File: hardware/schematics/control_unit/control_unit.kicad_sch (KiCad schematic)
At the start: 10 parts, among them J1 Screw_Terminal_01x12, J2 Screw_Terminal_01x08, J3 Screw_Terminal_01x08, J4 AudioJack4, J5 Screw_Terminal_01x08, J6 6P6C, J7 Conn_01x03_Pin, J8 Conn_01x03_Pin

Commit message: !feat
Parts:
- added H1, H2, H3, H4: MountingHole, MountingHole:MountingHole_4.5mm_Pad_TopBottom, symbol Mechanical:MountingHole
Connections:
- net GND: now also JP1.3 (B); no longer JP1.1 (A)
- net MCU/DE/~{RE}: now also JP1.1 (A); no longer JP1.3 (B)

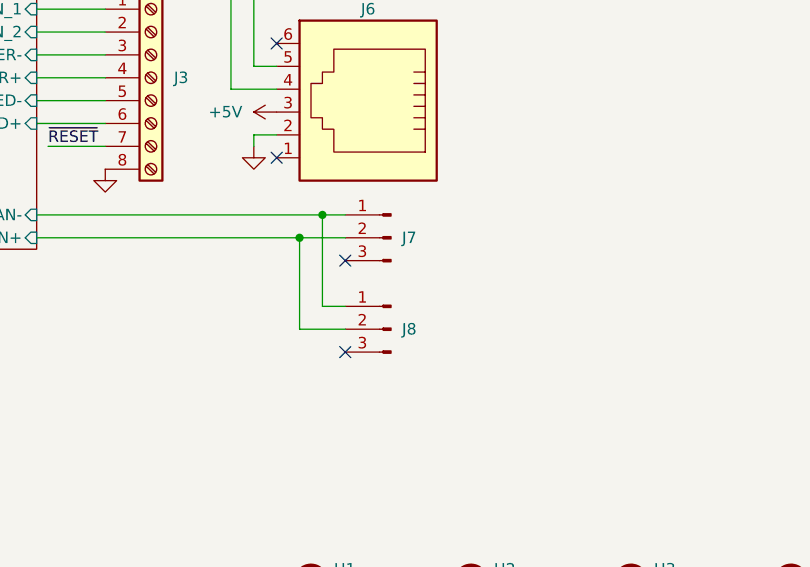
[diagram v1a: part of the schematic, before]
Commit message: feat: final PCB topological design.
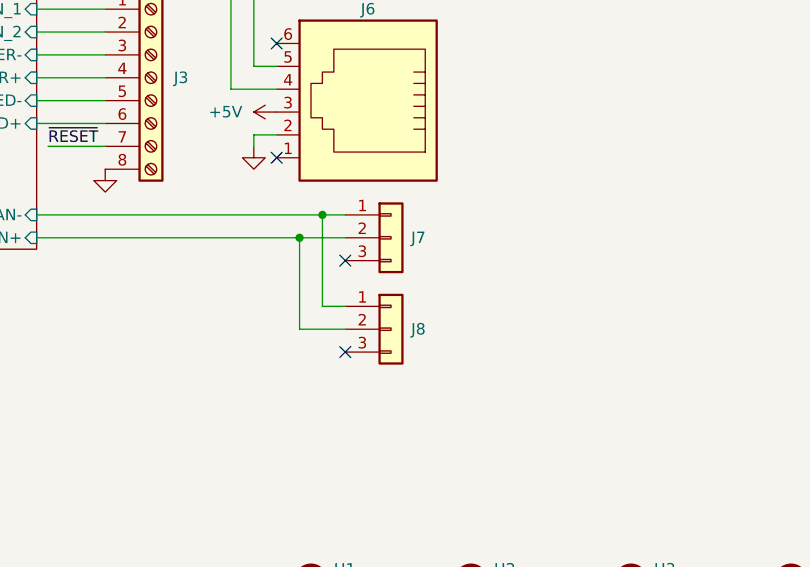
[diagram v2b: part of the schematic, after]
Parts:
- J7, J8: symbol Connector:Conn_01x03_Pin -> Connector_Generic:Conn_01x03
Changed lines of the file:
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@@
 	)
 	(symbol
-		(lib_id "Connector:Conn_01x03_Pin")
+		(lib_id "Connector_Generic:Conn_01x03")
 		(at 187.96 124.46 0)
-		(mirror y)
 		(unit 1)
 		(exclude_from_sim no)
@@
 		(dnp no)
 		(property "Reference" "J7"
-			(at 189.992 124.46 0)
+			(at 191.008 124.46 0)
 			(effects
 				(font
@@
 		)
 		(property "Value" "Conn_01x03_Pin"
-			(at 187.325 119.38 0)
+			(at 188.595 119.38 0)
 			(effects
 				(font
@@
 			)
 		)
-		(property "Description" "Generic connector, single row, 01x03, script generated"
+		(property "Description" "Generic connector, single row, 01x03, script generated (kicad-library-utils/schlib/autogen/connector/)"
 			(at 187.96 124.46 0)
 			(effects
@@
 	)
 	(symbol
-		(lib_id "Connector:Conn_01x03_Pin")
+		(lib_id "Connector_Generic:Conn_01x03")
 		(at 187.96 134.62 0)
-		(mirror y)
 		(unit 1)
 		(exclude_from_sim no)
@@
 		(dnp no)
 		(property "Reference" "J8"
-			(at 189.992 134.62 0)
+			(at 191.008 134.62 0)
 			(effects
 				(font
@@
 		)
 		(property "Value" "Conn_01x03_Pin"
-			(at 187.325 129.54 0)
+			(at 188.595 129.54 0)
 			(effects
 				(font
@@
 			)
 		)
-		(property "Description" "Generic connector, single row, 01x03, script generated"
+		(property "Description" "Generic connector, single row, 01x03, script generated (kicad-library-utils/schlib/autogen/connector/)"
 			(at 187.96 134.62 0)
 			(effects

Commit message: !feat: control_unit first PCB release.
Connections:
- net GND: now also J5.5 (Pin_5), J5.7 (Pin_7)
- net at F1.1, J5.3 (Pin_3): no longer J5.5 (Pin_5), J5.7 (Pin_7)
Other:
- moved on the sheet: F1
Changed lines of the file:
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@@
+	)
+	(junction
+		(at 165.1 36.83)
+		(diameter 0)
+		(color 0 0 0 0)
 	)
 	(junction
@@
 	)
 	(junction
-		(at 165.1 36.83)
-		(diameter 0)
-		(color 0 0 0 0)
-	)
-	(junction
 		(at 119.38 121.92)
 		(diameter 0)
@@
 	(wire
 		(pts
+			(xy 168.91 26.67) (xy 165.1 26.67)
+		)
+		(stroke
+			(width 0)
+			(type default)
+		)
+	)
+	(wire
+		(pts
 			(xy 165.1 41.91) (xy 176.53 41.91)
 		)
@@
 	(wire
 		(pts
+			(xy 165.1 26.67) (xy 165.1 27.94)
+		)
+		(stroke
+			(width 0)
+			(type default)
+		)
+	)
+	(wire
+		(pts
 			(xy 148.59 91.44) (xy 172.72 91.44)
 		)
@@
 	(wire
 		(pts
-			(xy 176.53 31.75) (xy 165.1 31.75)
-		)
-		(stroke
-			(width 0)
-			(type default)
-		)
-	)
-	(wire
-		(pts
 			(xy 53.34 44.45) (xy 63.5 44.45)
 		)
@@
 	(wire
 		(pts
+			(xy 168.91 31.75) (xy 168.91 26.67)
+		)
+		(stroke
+			(width 0)
+			(type default)
+		)
+	)
+	(wire
+		(pts
 			(xy 148.59 101.6) (xy 156.21 101.6)
 		)
@@
 	(wire
 		(pts
+			(xy 165.1 35.56) (xy 165.1 36.83)
+		)
+		(stroke
+			(width 0)
+			(type default)
+		)
+	)
+	(wire
+		(pts
 			(xy 177.8 124.46) (xy 182.88 124.46)
 		)
@@
 	(wire
 		(pts
-			(xy 167.64 26.67) (xy 176.53 26.67)
+			(xy 171.45 26.67) (xy 176.53 26.67)
 		)
 		(stroke
@@
 	(wire
 		(pts
-			(xy 167.64 29.21) (xy 176.53 29.21)
+			(xy 171.45 29.21) (xy 176.53 29.21)
 		)
 		(stroke
@@
 	(wire
 		(pts
+			(xy 176.53 31.75) (xy 168.91 31.75)
+		)
+		(stroke
+			(width 0)
+			(type default)
+		)
+	)
+	(wire
+		(pts
 			(xy 111.76 64.77) (xy 121.92 64.77)
 		)
@@
 	(wire
 		(pts
-			(xy 165.1 31.75) (xy 165.1 36.83)
-		)
-		(stroke
-			(width 0)
-			(type default)
-		)
-	)
-	(wire
-		(pts
 			(xy 165.1 41.91) (xy 165.1 45.72)
 		)
@@
 	)
 	(label "AC_N"
-		(at 167.64 29.21 0)
+		(at 171.45 29.21 0)
 		(fields_autoplaced yes)
 		(effects
@@
 	)
 	(label "AC_L"
-		(at 167.64 26.67 0)
+		(at 171.45 26.67 0)
 		(fields_autoplaced yes)
 		(effects
@@
 	(symbol
 		(lib_id "Device:Fuse")
-		(at 165.1 49.53 0)
+		(at 165.1 31.75 0)
+		(mirror y)
 		(unit 1)
 		(exclude_from_sim no)
@@
 		(on_board yes)
 		(dnp no)
-		(fields_autoplaced yes)
 		(property "Reference" "F1"
-			(at 167.64 48.2599 0)
+			(at 162.56 30.4799 0)
 			(effects
 				(font
@@
 		)
 		(property "Value" "T30A 250V"
-			(at 167.64 50.7999 0)
+			(at 162.56 33.0199 0)
 			(effects
 				(font
@@
 		)
 		(property "Footprint" "Fuse:Fuseholder_Clip-6.3x32mm_Littelfuse_102_Inline_P34.21x7.62mm_D2.54mm_Horizontal"
-			(at 163.322 49.53 90)
+			(at 166.878 31.75 90)
 			(effects
 				(font
@@
 		)
 		(property "Datasheet" "~"
-			(at 165.1 49.53 0)
+			(at 165.1 31.75 0)
 			(effects
 				(font
@@
 		)
 		(property "Description" "Fuse"
-			(at 165.1 49.53 0)
+			(at 165.1 31.75 0)
 			(effects
 				(font
@@
 	(symbol
 		(lib_id "power:GND")
-		(at 165.1 53.34 0)
+		(at 165.1 45.72 0)
 		(unit 1)
 		(exclude_from_sim no)
@@
 		(fields_autoplaced yes)
 		(property "Reference" "#PWR019"
-			(at 165.1 59.69 0)
+			(at 165.1 52.07 0)
 			(effects
 				(font
@@
 		)
 		(property "Value" "GND"
-			(at 165.1 58.42 0)
+			(at 165.1 50.8 0)
 			(effects
 				(font
@@
 		)
 		(property "Footprint" ""
-			(at 165.1 53.34 0)
+			(at 165.1 45.72 0)
 			(effects
 				(font
@@
 		)
 		(property "Datasheet" ""
-			(at 165.1 53.34 0)
+			(at 165.1 45.72 0)
 			(effects
 				(font
@@
 		)
 		(property "Description" "Power symbol creates a global label with name \"GND\" , ground"
-			(at 165.1 53.34 0)
-			(effects
-				(font
+			(at 165.1 45.72 0)
+			(effects
+				(font

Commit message: chore
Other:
- sheet HOMEMONITOR renamed POWERMONITOR
- sheet POWERMONITOR: file untitled.kicad_sch -> powermonitor.kicad_sch
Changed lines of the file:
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@@
 			(color 255 255 194 1.0000)
 		)
-		(property "Sheetname" "HOMEMONITOR"
+		(property "Sheetname" "POWERMONITOR"
 			(at 63.5 37.3884 0)
 			(effects
@@
 			)
 		)
-		(property "Sheetfile" "untitled.kicad_sch"
+		(property "Sheetfile" "powermonitor.kicad_sch"
 			(at 63.5 56.4646 0)
 			(effects

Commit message: fix
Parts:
- J4: footprint HomeMonitor:SCT013 -> PowerMonitor:SCT013
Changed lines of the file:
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@@
 			)
 		)
-		(property "Footprint" "HomeMonitor:SCT013"
+		(property "Footprint" "PowerMonitor:SCT013"
 			(at 176.53 66.04 0)
 			(effects

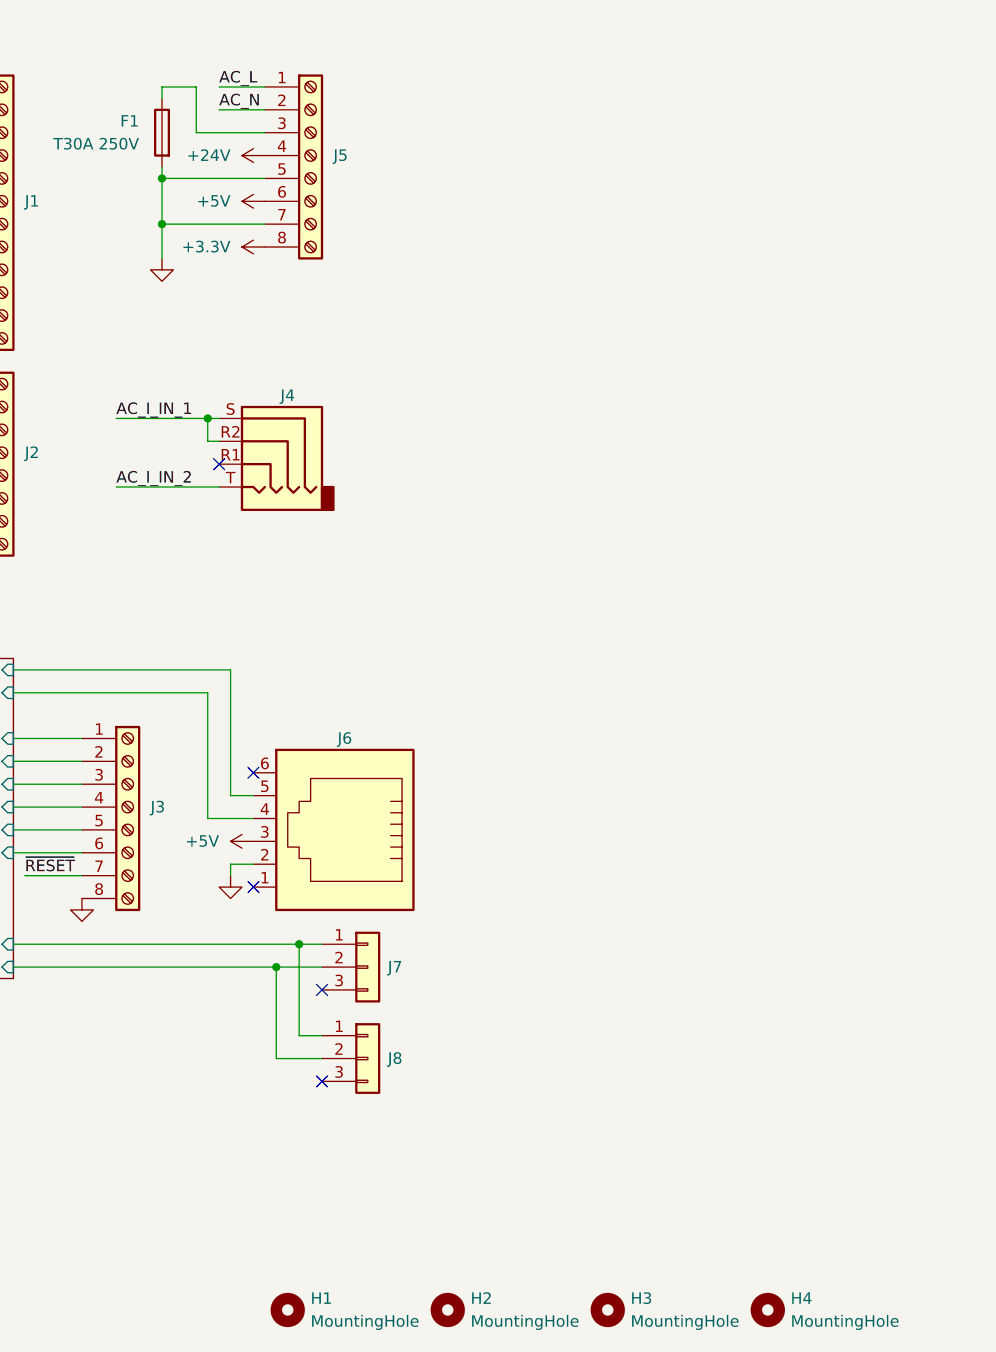
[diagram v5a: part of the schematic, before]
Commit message: feat: screw to fuse-
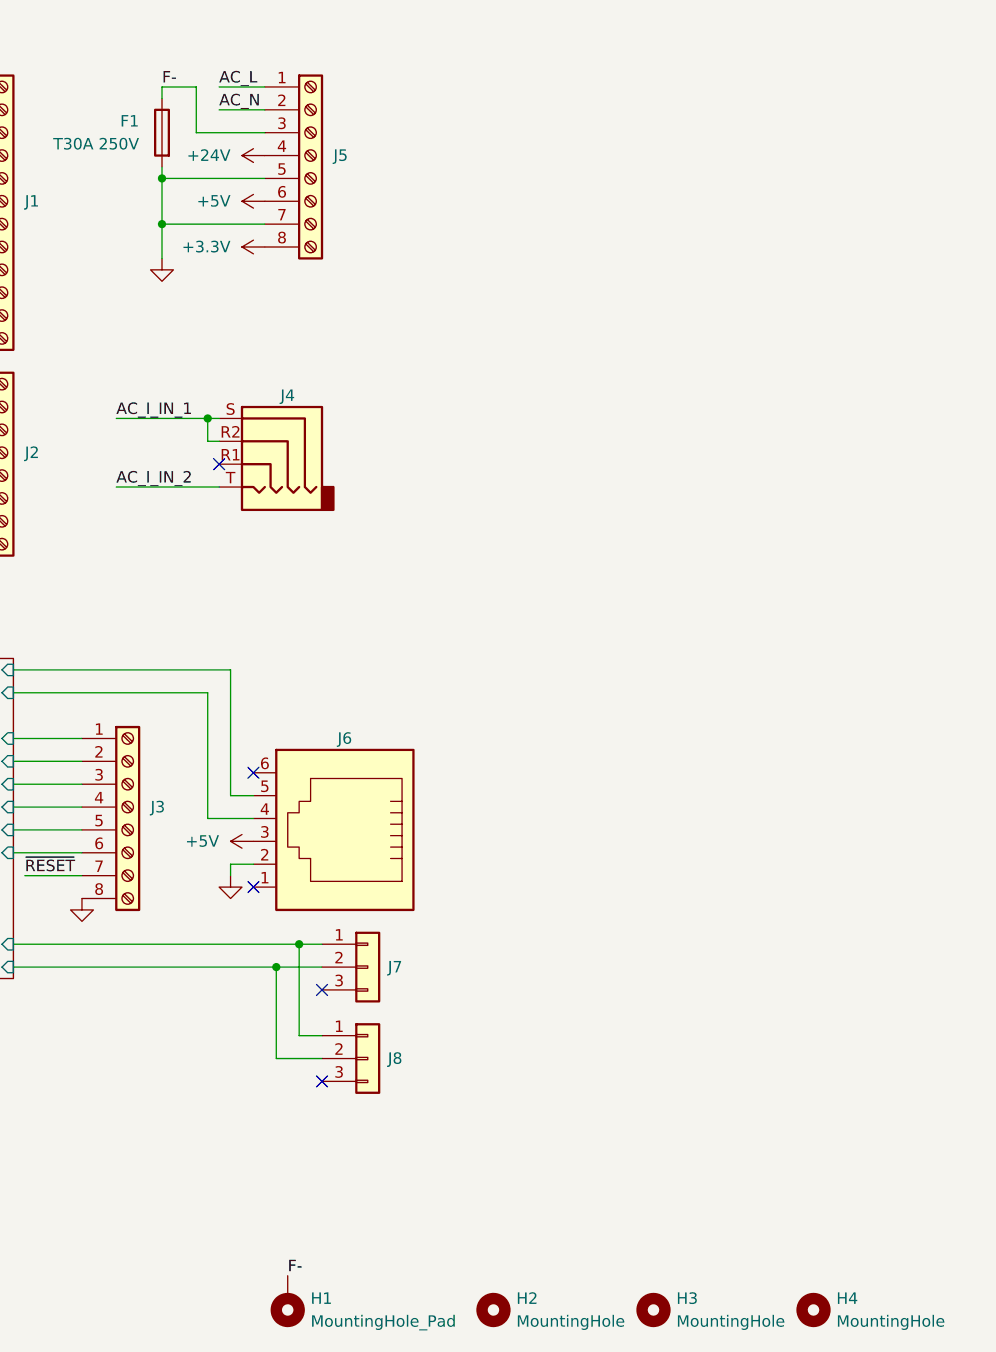
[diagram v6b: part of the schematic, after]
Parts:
- removed H1: MountingHole, MountingHole:MountingHole_4.5mm_Pad_TopBottom, symbol Mechanical:MountingHole
- added H1: MountingHole_Pad, MountingHole:MountingHole_4.5mm_Pad_TopBottom, symbol Mechanical:MountingHole_Pad
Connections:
- net F-: now reaches F1.1, J5.3 (Pin_3)
- net F-: now also H1.1
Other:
- moved on the sheet: H2, H3, H4

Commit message: docs
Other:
- note added: "!!! AGGIUNGERE ACCESSO AD UART CON STRIPLINE Applique 4 LED di fila: 36V @ 102.5mA A gruppi di due, è stata messa una resistenza da 56 Ohm, 1W."
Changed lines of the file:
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@@
 		(title "Domoticata main control unit")
 		(date "2024-07-14")
-		(rev "0.1")
+		(rev "0.0.1")
 		(company "Davide Scalisi")
 	)
@@
 		)
 	)
+	(text "!!! AGGIUNGERE ACCESSO AD UART CON STRIPLINE\n\nApplique 4 LED di fila: 36V @ 102.5mA\nA gruppi di due, è stata messa una resistenza da 56 Ohm, 1W."
+		(exclude_from_sim no)
+		(at 51.054 95.25 0)
+		(effects
+			(font
+				(size 1.27 1.27)
+			)
+		)
+	)
